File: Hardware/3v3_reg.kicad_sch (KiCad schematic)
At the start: 3 parts, among them U3 AP2112K-3.3

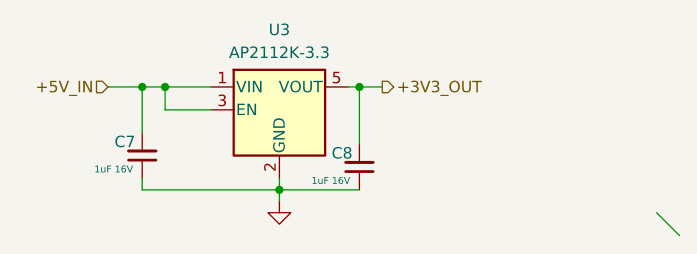
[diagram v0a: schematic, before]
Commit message: Finalize schematic: Add connectors, LEDs, Buzzer and fix all ERC errors
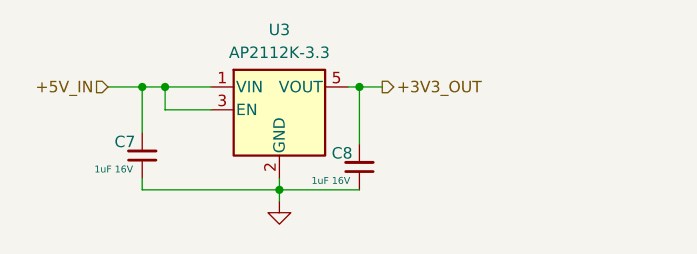
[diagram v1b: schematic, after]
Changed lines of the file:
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@@
 		(color 0 0 0 0)
-	)
-	(bus_entry
-		(at 182.88 83.82)
-		(size 2.54 2.54)
-		(stroke
-			(width 0)
-			(type default)
-		)
 	)
 	(wire

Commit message: Finalize component placement and silkscreen
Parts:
- C7, C8: footprint (none) -> Capacitor_SMD:C_0402_1005Metric
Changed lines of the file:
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@@
 			)
 		)
-		(property "Footprint" ""
+		(property "Footprint" "Capacitor_SMD:C_0402_1005Metric"
 			(at 149.86 78.74 0)
 			(effects
@@
 			)
 		)
-		(property "Footprint" ""
+		(property "Footprint" "Capacitor_SMD:C_0402_1005Metric"
 			(at 125.73 77.47 0)
 			(effects
